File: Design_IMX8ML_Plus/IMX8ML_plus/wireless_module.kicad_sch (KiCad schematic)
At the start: 1 part

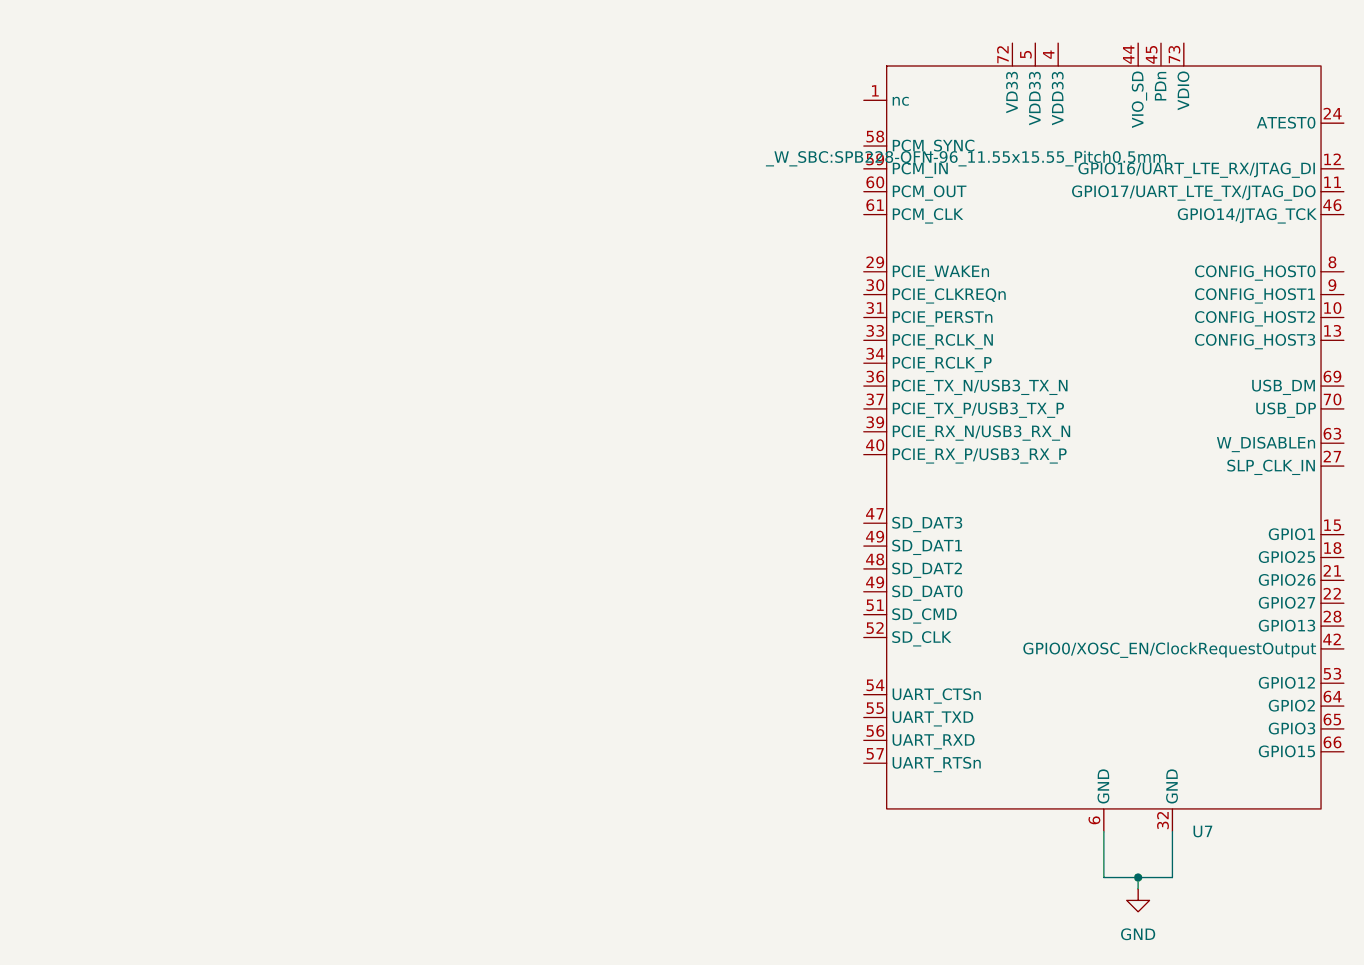
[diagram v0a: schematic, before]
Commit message: Improve power source module in the base board
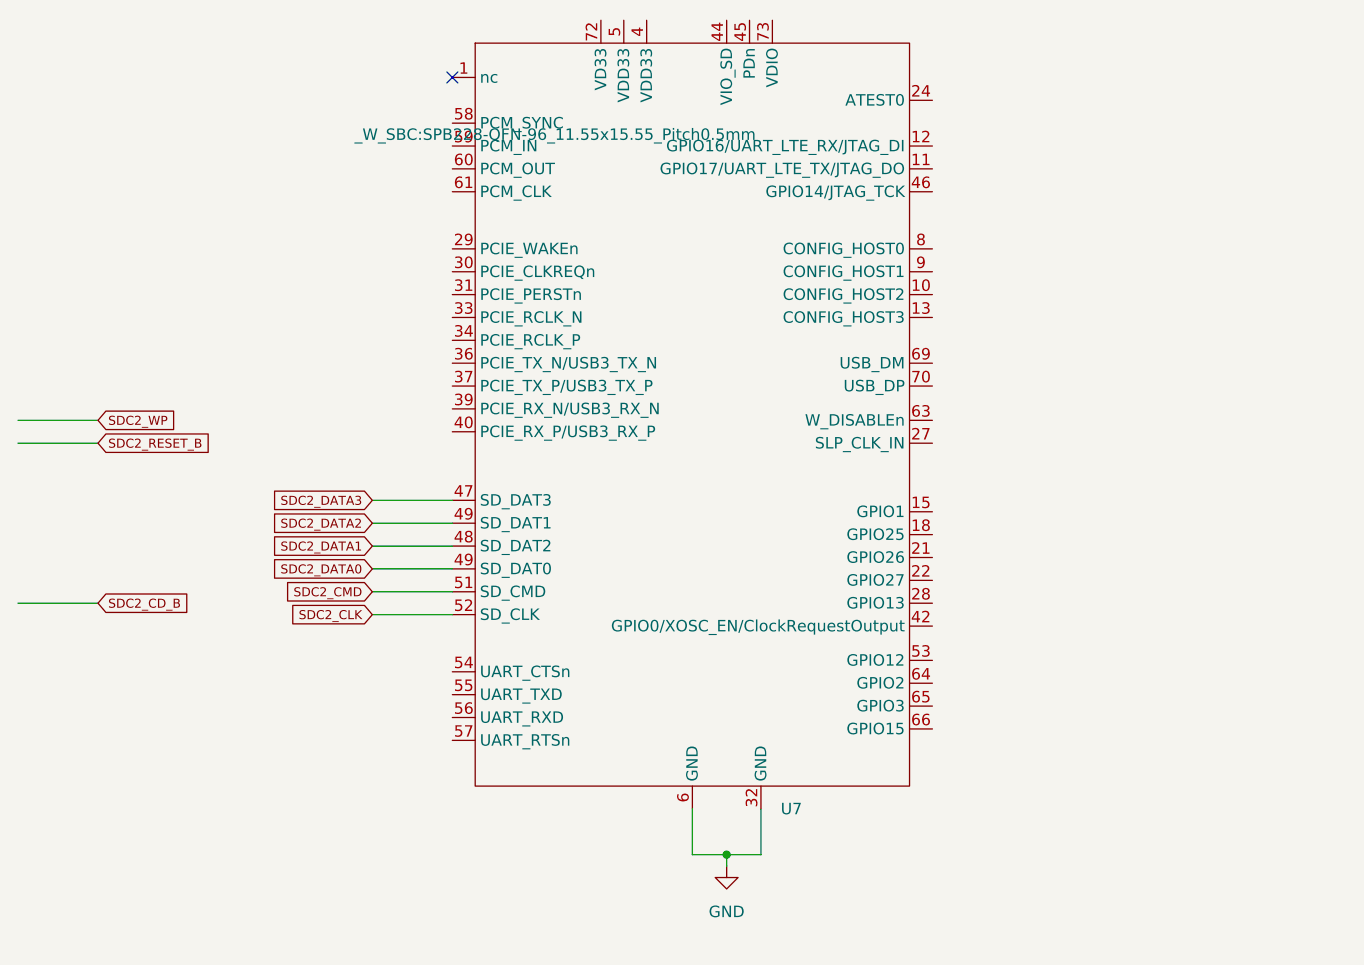
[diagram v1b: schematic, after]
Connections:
- net SDC2_DATA3: now reaches U7.47 (SD_DAT3)
- net SDC2_DATA1: now reaches U7.48 (SD_DAT2)
- net SDC2_DATA2: now reaches U7.49 (SD_DAT1)
- net SDC2_CMD: now reaches U7.51 (SD_CMD)
- net SDC2_CLK: now reaches U7.52 (SD_CLK)
- new net SDC2_DATA0: U7.49 (SD_DAT1)
- no-connect marks 0 -> 1
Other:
- moved on the sheet: U7

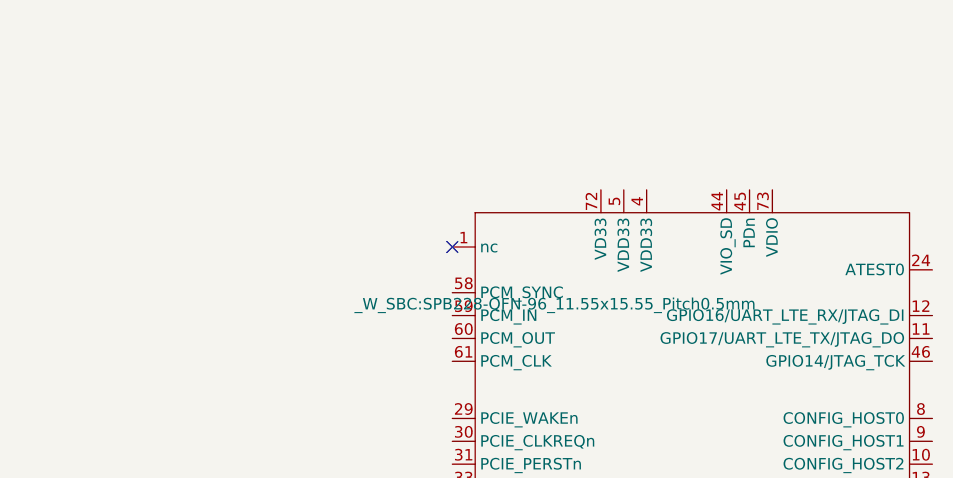
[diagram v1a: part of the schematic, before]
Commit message: reorganization of the componentes
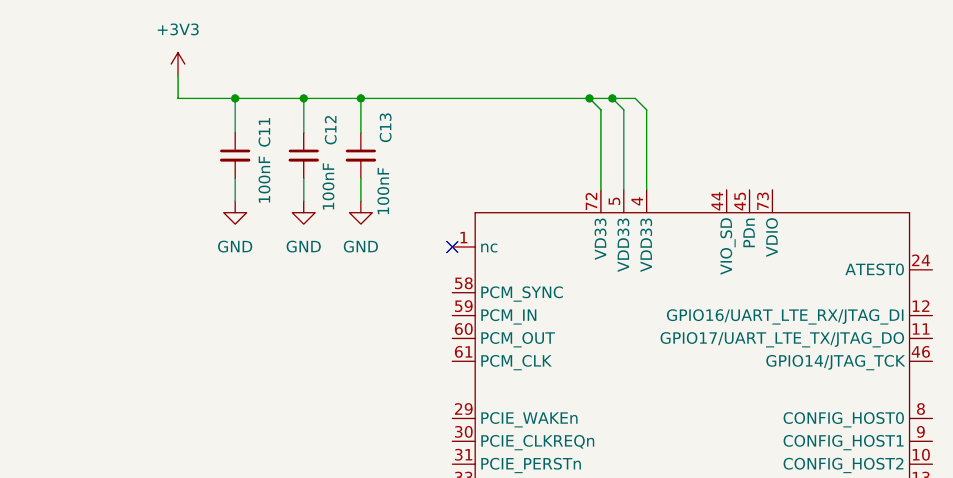
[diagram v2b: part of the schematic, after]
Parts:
- added C11, C12, C13: 100nF, Capacitor_SMD:C_0201_0603Metric_Pad0.64x0.40mm_HandSolder, symbol Device:C_Small
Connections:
- net GND: now also C11.2, C12.2, C13.2
- net +3V3: now reaches U7.4 (VDD33)
- net +3V3: now also U7.5 (VDD33), U7.72 (VD33), C11.1, C12.1, C13.1

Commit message: [PROCESSOR] Create zones It added power zones in the four layer
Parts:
- renumbered C11 to C154, C12 to C155, C13 to C156
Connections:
- net SDC2_DATA2 is gone; now on net SDC1_DATA1: U7.49 (SD_DAT1)
- net UART1_RTS: now reaches U7.54 (UART_CTSn)
- net UART1_CTS: now reaches U7.55 (UART_TXD)
- net UART1_TXD: now reaches U7.56 (UART_RXD)
- net UART1_RXD: now reaches U7.57 (UART_RTSn)
- net SDC2_CLK renamed SDC1_CLK
- net SDC2_CMD renamed SDC1_CMD
- net SDC2_DATA0 renamed SDC1_DATA1
- net SDC2_DATA1 renamed SDC1_DATA2
- net SDC2_DATA3 renamed SDC1_DATA3
- new net SDC1_DATA0: U7.50 (SD_DAT0)

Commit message: [CPU/BB] Improving the conection between the cpu and BB
* Reorganization of the components in the Base board.
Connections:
- net UART1_CTS renamed UART3_RXD
- net UART1_RTS renamed UART3_RTS
- net UART1_RXD renamed UART3_CTS
- net UART1_TXD renamed UART3_TXD
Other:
- note added: "SD1_DATA6"
- note added: "SD1_DATA7"
- note added: "SD1_RESET_B"
- note added: "SD1_STROBE"
- moved on the sheet: C154, C155, C156, U7

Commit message: [BB_IMX8MLP IMX8MLP] Actuallizated to 9.0 kicad version
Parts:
- C154, C155, C156: footprint Capacitor_SMD:C_0201_0603Metric_Pad0.64x0.40mm_HandSolder -> Capacitor_SMD:C_0201_0603Metric
- U7: MP (none) -> -
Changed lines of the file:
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@@
 (kicad_sch
-	(version 20231120)
+	(version 20250114)
 	(generator "eeschema")
-	(generator_version "8.0")
+	(generator_version "9.0")
 	(paper "A4")
+	(text "SD1_DATA7"
+		(exclude_from_sim no)
+		(at 86.614 138.684 0)
+		(effects
+			(font
+				(size 1.27 1.27)
+			)
+		)
+	)
+	(text "SD1_RESET_B"
+		(exclude_from_sim no)
+		(at 85.852 135.89 0)
+		(effects
+			(font
+				(size 1.27 1.27)
+			)
+		)
+	)
+	(text "SD1_STROBE"
+		(exclude_from_sim no)
+		(at 86.36 143.764 0)
+		(effects
+			(font
+				(size 1.27 1.27)
+			)
+		)
+	)
+	(text "SD1_DATA6"
+		(exclude_from_sim no)
+		(at 86.868 141.224 0)
+		(effects
+			(font
+				(size 1.27 1.27)
+			)
+		)
+	)
 	(junction
 		(at 87.63 53.34)
@@
 			(width 0)
 			(type default)
-		)
-	)
-	(text "SD1_DATA7"
-		(exclude_from_sim no)
-		(at 86.614 138.684 0)
-		(effects
-			(font
-				(size 1.27 1.27)
-			)
-		)
-	)
-	(text "SD1_RESET_B"
-		(exclude_from_sim no)
-		(at 85.852 135.89 0)
-		(effects
-			(font
-				(size 1.27 1.27)
-			)
-		)
-	)
-	(text "SD1_STROBE"
-		(exclude_from_sim no)
-		(at 86.36 143.764 0)
-		(effects
-			(font
-				(size 1.27 1.27)
-			)
-		)
-	)
-	(text "SD1_DATA6"
-		(exclude_from_sim no)
-		(at 86.868 141.224 0)
-		(effects
-			(font
-				(size 1.27 1.27)
-			)
 		)
 	)
@@
 			)
 		)
-		(property "Footprint" "Capacitor_SMD:C_0201_0603Metric_Pad0.64x0.40mm_HandSolder"
+		(property "Footprint" "Capacitor_SMD:C_0201_0603Metric"
 			(at 101.6 59.69 0)
 			(effects
@@
 			)
 		)
-		(property "Footprint" "Capacitor_SMD:C_0201_0603Metric_Pad0.64x0.40mm_HandSolder"
+		(property "Footprint" "Capacitor_SMD:C_0201_0603Metric"
 			(at 87.63 59.69 0)
 			(effects
@@
 			)
 		)
-		(property "Footprint" "Capacitor_SMD:C_0201_0603Metric_Pad0.64x0.40mm_HandSolder"
+		(property "Footprint" "Capacitor_SMD:C_0201_0603Metric"
 			(at 95.25 59.69 0)
 			(effects
@@
 			(at 123.19 76.2 0)
 			(effects
+				(font
+					(size 1.27 1.27)
+				)
+				(hide yes)
+			)
+		)
+		(property "MP" "-"
+			(at 123.19 76.2 0)
+			(effects

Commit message: [IMX8ML] Add new layer
A new layers was add in the cpu schematic, now it had 8 layer.
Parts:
- U7: value ~ -> (none)
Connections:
- net UART3_CTS renamed UART3_CTS_WiFi
- net UART3_RTS renamed UART3_RTS_WiFi
- net UART3_RXD renamed UART3_RXD_WiFi
- net UART3_TXD renamed UART3_TXD_WiFi
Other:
- note added: "CONFIG WLAN BLE 000 SDIO UART 001 SDIO SDIO 010 PCIe USB2.0 011 PCIe UART 100 USB3.0/2.0 UART 101 USB.0 USB2.0 110 USB3.0/2.0 USB3.0/2.0 111 USB3.0 USB3.0 CONFIGx Connect 100 kohm to GND to set the signal to "0" PDn Power Down Input (active low), Pulling PDn pin low, sets SPB228 in Standby mode. This turns OFF most parts of the circuit and minimizes the current consumption. All I/O interface pins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"
- moved on the sheet: C154, C155, C156, U7
